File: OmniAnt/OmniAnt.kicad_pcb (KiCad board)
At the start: 2 copper layers, 1 part, among them U1 ESP32-S3-WROOM-1

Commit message: Mostly organizing
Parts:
- added C1: 1uF, PCM_JLCPCB:C_0603, F.Cu at (-115.2, 17.5)
- added C11: 1uF, PCM_JLCPCB:C_0603, F.Cu at (-115.2, 24.2)
- added C14: 1uF, PCM_JLCPCB:C_0603, F.Cu at (-115.2, 26.5)
- added C15: 100nF, PCM_JLCPCB:C_0603, F.Cu at (-115.2, 37.5)
- added C19: 1uF, PCM_JLCPCB:C_0603, F.Cu at (-115.2, 28.8)
- added C2: 1uF, PCM_JLCPCB:C_0603, F.Cu at (-115.2, 19.8)
- added C20: 1uF, PCM_JLCPCB:C_0603, F.Cu at (-115.2, 31.0)
- added C21: 100nF, PCM_JLCPCB:C_0603, F.Cu at (-115.2, 33.2)
- added C22: 100nF, PCM_JLCPCB:C_0603, F.Cu at (-115.2, 39.8)
- added C23: 100nF, PCM_JLCPCB:C_0603, F.Cu at (-115.2, 42.0)
- added C4: 470pF, PCM_JLCPCB:C_0603, F.Cu at (-115.2, 22.0)
- added C6: 10uF, PCM_JLCPCB:C_0805, F.Cu at (-108.2, 27.5)
- added C7: 10uF, PCM_JLCPCB:C_0805, F.Cu at (-111.1, 43.5)
- added C8: 10uF, PCM_JLCPCB:C_0805, F.Cu at (-108.2, 30.5)
- added D1: PMEG100V080ELPD, Package_TO_SOT_SMD:Nexperia_CFP15_SOT-1289, F.Cu at (-56.0, 42.9)
- added J1: Conn_01x02_Pin, Connector_PinHeader_1.27mm:PinHeader_1x02_P1.27mm_Vertical, F.Cu at (-62.6, 44.1)
- added J3: Connector, USB-TYPE-C-16P, PCM_JLCPCB:TYPE-C-SMD_HX-TYPE-C-16PIN, F.Cu at (-54.8, 34.0)
- added Q10: NTMFS4C324NT1G, Footprints:NVMFS5C442NLWFAFT1G, F.Cu at (-91.7, 21.2)
- added Q11: NTMFS4C324NT1G, Footprints:NVMFS5C442NLWFAFT1G, F.Cu at (-83.0, 21.2)
- added Q12: NTMFS4C324NT1G, Footprints:NVMFS5C442NLWFAFT1G, F.Cu at (-74.4, 21.2)
- added Q7: NTMFS4C324NT1G, Footprints:NVMFS5C442NLWFAFT1G, F.Cu at (-64.0, 21.7)
- added Q8: NTMFS4C324NT1G, Footprints:NVMFS5C442NLWFAFT1G, F.Cu at (-109.0, 21.2)
- added Q9: NTMFS4C324NT1G, Footprints:NVMFS5C442NLWFAFT1G, F.Cu at (-100.3, 21.2)
- added R1: 10kΩ, PCM_JLCPCB:R_0402, F.Cu at (-111.9, 37.3)
- added R10: 5.1kΩ, PCM_JLCPCB:R_0402, F.Cu at (-111.9, 32.4)
- added R11: 5.1kΩ, PCM_JLCPCB:R_0402, F.Cu at (-111.9, 39.1)
- added R12: 5.1kΩ, PCM_JLCPCB:R_0402, F.Cu at (-111.9, 41.0)
- added R3: 10kΩ, PCM_JLCPCB:R_0402, F.Cu at (-111.9, 26.9)
- added R4: 10kΩ, PCM_JLCPCB:R_0402, F.Cu at (-111.9, 28.7)
- added R6: 2m, Resistor_SMD:R_1206_3216Metric, F.Cu at (-35.3, 32.0)
- added R9: 5.1kΩ, PCM_JLCPCB:R_0402, F.Cu at (-111.9, 30.6)
- added U2: TPSM53603RDA, Package_DFN_QFN:Texas_B3QFN-14-1EP_5x5.5mm_P0.65mm_ThermalVia, F.Cu at (-48.0, 43.3)
- added U3: MCF8329A1IREER, Footprints:REE0036A-MFG, F.Cu at (8.50, 144.0)
- added U4: USBLC6-2P6, Package_TO_SOT_SMD:SOT-666, F.Cu at (-58.2, 47.6)
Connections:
- U1 pad 12: unconnected-(U1-IO8-Pad12) -> /MotorController_MCF8329A/SDA
- U1 pad 13: unconnected-(U1-USB_D--Pad13) -> /D-
- U1 pad 14: unconnected-(U1-USB_D+-Pad14) -> /D+
- U1 pad 17: unconnected-(U1-IO9-Pad17) -> /MotorController_MCF8329A/SCL
- U1 pad 2: unconnected-(U1-3V3-Pad2) -> +3.3V
- U1 pad 27: unconnected-(U1-IO0-Pad27) -> Net-(J1-Pin_1)
- U1 pad 4: unconnected-(U1-IO4-Pad4) -> /MotorController_MCF8329A/DACOut

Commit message: Good progress on the power stage today.
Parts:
- removed D1: PMEG100V080ELPD, Package_TO_SOT_SMD:Nexperia_CFP15_SOT-1289
- added D2: SSL34F, PCM_JLCPCB:D_SMAF, F.Cu at (-96.5, 99.0)
- moved Q8 34.6 mm to (-74.4, 19.5)
- moved Q7 15.1 mm to (-74.4, 10.7)
- moved Q12 13.4 mm to (-87.5, 18.7)
- moved Q11 11.9 mm to (-87.5, 10.2)
- moved Q9 8.46 mm to (-98.1, 13.0)
- moved Q10 6.68 mm to (-98.1, 23.0)

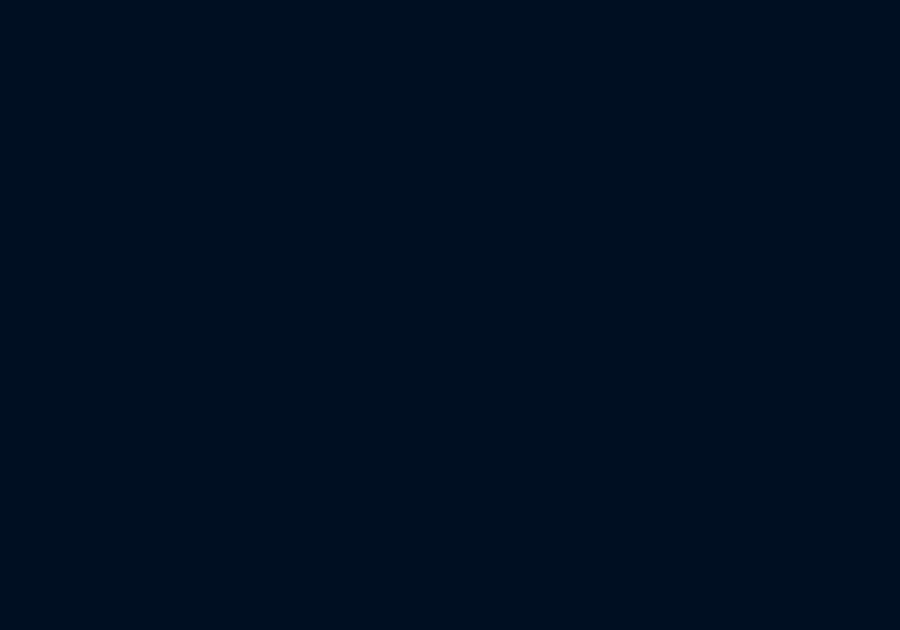
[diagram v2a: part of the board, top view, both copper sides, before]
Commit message: I added a green LED.
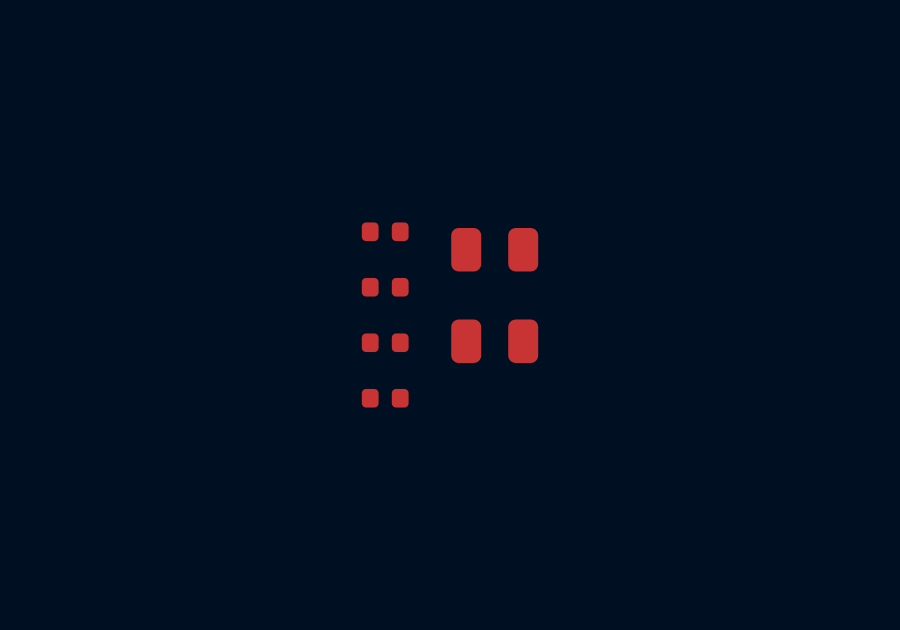
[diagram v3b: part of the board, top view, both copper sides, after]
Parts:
- added C10: 10uF, PCM_JLCPCB:C_0805, F.Cu at (-5.35, 34.1)
- added C9: 10uF, PCM_JLCPCB:C_0805, F.Cu at (-5.35, 31.1)
- added R13: 5.1kΩ, PCM_JLCPCB:R_0402, F.Cu at (-9.00, 34.1)
- added R14: 5.1kΩ, PCM_JLCPCB:R_0402, F.Cu at (-9.00, 36.0)
- added R2: 5.1kΩ, PCM_JLCPCB:R_0402, F.Cu at (-9.00, 30.4)
- added R5: 12kΩ, PCM_JLCPCB:R_0402, F.Cu at (-9.00, 32.3)
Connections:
- C23 pad 1: Net-(J2-VBUS) -> /VUSB
- D2 pad 1: /VUSB -> /Batt
- D2 pad 2: Net-(J2-VBUS) -> /VUSB
- J3 pad A12B1: Net-(J3-GND-PadA12B1) -> GND
- J3 pad A5: unconnected-(J3-CC1-PadA5) -> Net-(J3-CC1)
- J3 pad A6: unconnected-(J3-D+-PadA6) -> Net-(J3-D+-PadA6)
- J3 pad A7: unconnected-(J3-D--PadA7) -> Net-(J3-D--PadA7)
- J3 pad A9B4: Net-(J3-VBUS-PadA9B4) -> /VUSB
- J3 pad B12A1: Net-(J3-GND-PadA12B1) -> GND
- J3 pad B5: unconnected-(J3-CC2-PadB5) -> Net-(J3-CC2)
- J3 pad B6: unconnected-(J3-D+-PadB6) -> Net-(J3-D+-PadA6)
- J3 pad B7: unconnected-(J3-D--PadB7) -> Net-(J3-D--PadA7)
- J3 pad B9A4: Net-(J3-VBUS-PadA9B4) -> /VUSB
- J3 pad S1: unconnected-(J3-SHIELD-PadS1) -> GND
- R11 pad 1: /MotorController_MCF8329A/SCL -> /I2C_SCL
- R12 pad 1: /MotorController_MCF8329A/SDA -> /I2C_SDA
- U1 pad 10: unconnected-(U1-IO17-Pad10) -> /Motor1_PWM
- U1 pad 11: unconnected-(U1-IO18-Pad11) -> /Motor2_PWM
- U1 pad 12: /MotorController_MCF8329A/SDA -> unconnected-(U1-IO8-Pad12)
- U1 pad 17: /MotorController_MCF8329A/SCL -> unconnected-(U1-IO9-Pad17)
- U1 pad 23: unconnected-(U1-IO21-Pad23) -> /Motor3_PWM
- U1 pad 24: unconnected-(U1-IO47-Pad24) -> /I2C_SDA
- U1 pad 25: unconnected-(U1-IO48-Pad25) -> /I2C_SCL
- U1 pad 32: unconnected-(U1-IO39-Pad32) -> /SPI1_MOSI
- U1 pad 33: unconnected-(U1-IO40-Pad33) -> /SPI1_MISO
- U1 pad 34: unconnected-(U1-IO41-Pad34) -> /SPI1_SCK
- U1 pad 35: unconnected-(U1-IO42-Pad35) -> /SPI1_CS
- U1 pad 38: unconnected-(U1-IO2-Pad38) -> /Motor2_DAC
- U1 pad 39: unconnected-(U1-IO1-Pad39) -> /Motor1_DAC
- U1 pad 4: /MotorController_MCF8329A/DACOut -> /Motor3_DAC
- U2 pad 1: Net-(U2-VIN-Pad1) -> /Batt
- U2 pad 10: Net-(U2-PGND-Pad10) -> GND
- U2 pad 11: Net-(U2-PGND-Pad10) -> GND
- U2 pad 12: unconnected-(U2-AGND-Pad12) -> GND
- U2 pad 14: Net-(U2-VIN-Pad1) -> /Batt
- U2 pad 15: Net-(U2-PGND-Pad10) -> GND
- U2 pad 2: unconnected-(U2-EN-Pad2) -> /Batt
- U2 pad 3: Net-(U2-PGND-Pad10) -> GND
- U2 pad 7: Net-(U2-VOUT-Pad7) -> +3.3V
- U2 pad 8: Net-(U2-VOUT-Pad7) -> +3.3V
- U2 pad 9: unconnected-(U2-FB-Pad9) -> Net-(U2-FB)
- U3 pad 27: /MotorController_MCF8329A/3.3V -> /Motor1_PWM
- U3 pad 29: /MotorController_MCF8329A/SDA -> /MotorController_MCF8329A/I2C_SDA
- U3 pad 30: /MotorController_MCF8329A/SCL -> /MotorController_MCF8329A/I2C_SCL
- U3 pad 33: /MotorController_MCF8329A/DACOut -> /Motor1_DAC
- U4 pad 1: Net-(J2-D-) -> Net-(J3-D+-PadA6)
- U4 pad 2: Net-(J2-VBUS) -> /VUSB
- U4 pad 3: Net-(J2-D+) -> Net-(J3-D--PadA7)
- U4 pad 4: /D+ -> /D-
- U4 pad 6: /D- -> /D+

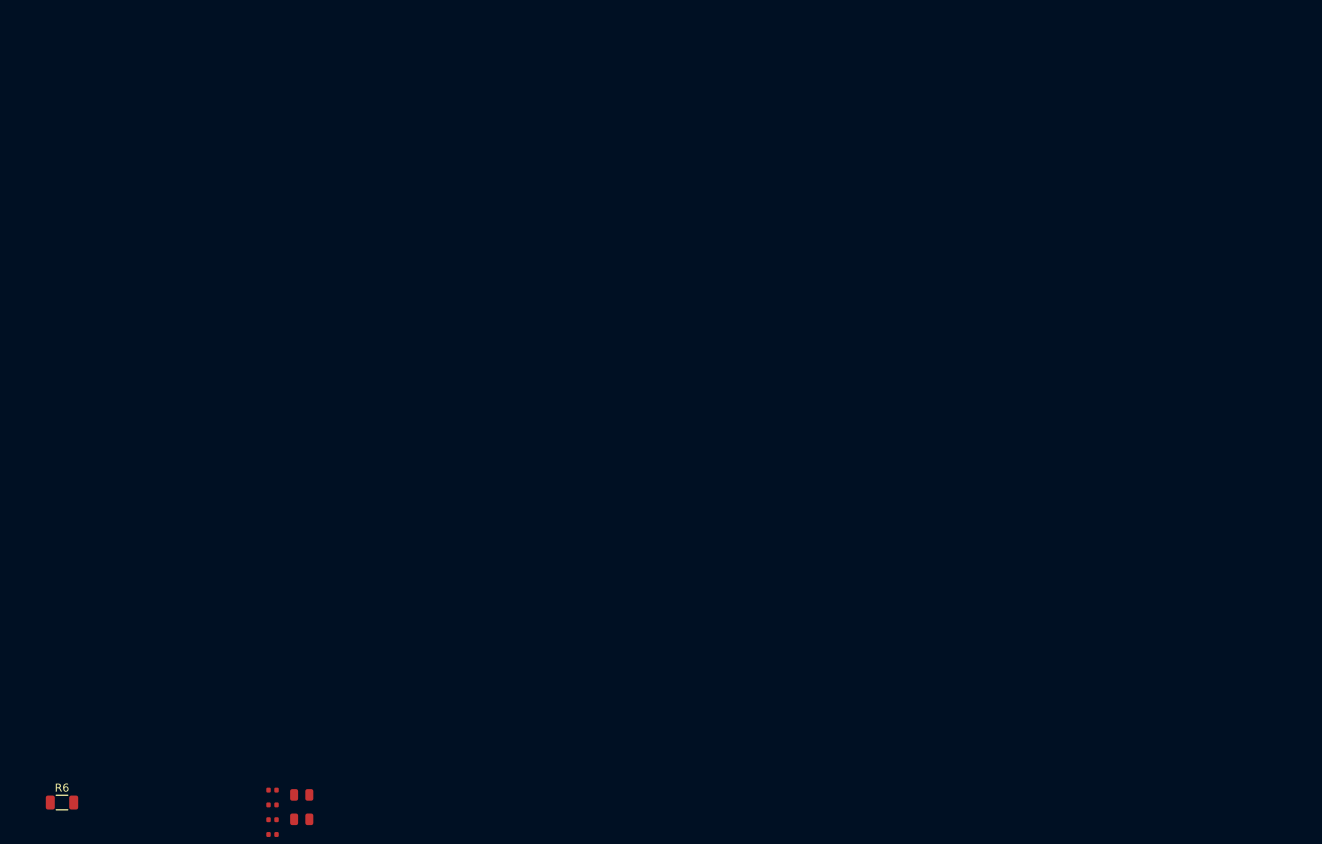
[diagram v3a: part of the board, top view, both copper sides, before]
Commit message: I added in the XT30 Connectors for the batteries
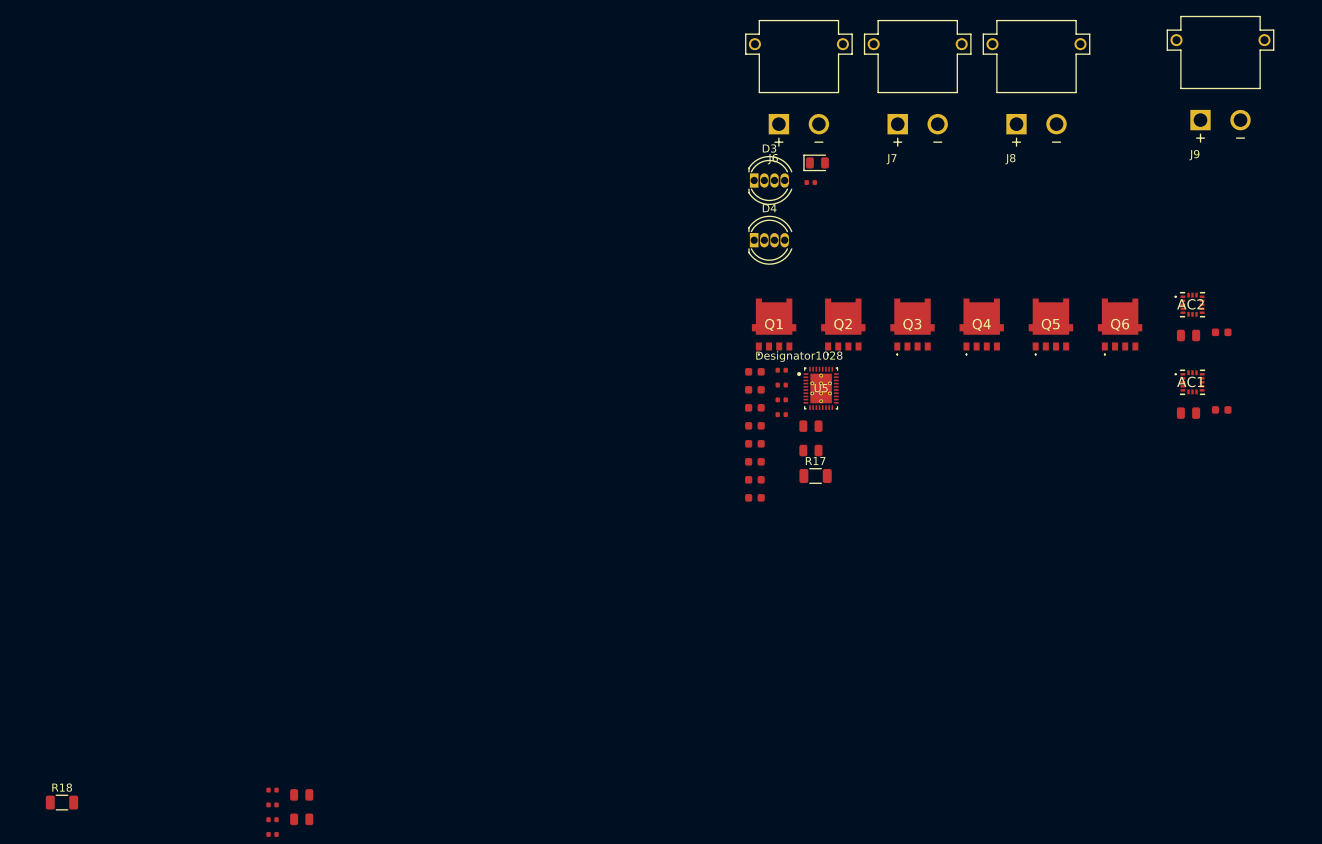
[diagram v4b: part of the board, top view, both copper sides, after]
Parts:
- added AC1: H3LIS331DL, Footprints:LIS3DHTR, F.Cu at (106.0, -20.5)
- added AC2: H3LIS331DL, Footprints:LIS3DHTR, F.Cu at (106.0, -30.2)
- added C1: 10uF, PCM_JLCPCB:C_0805, F.Cu at (105.5, -16.7)
- added C12: 10uF, PCM_JLCPCB:C_0805, F.Cu at (58.3, -15.0)
- added C13: 10uF, PCM_JLCPCB:C_0805, F.Cu at (58.3, -12.0)
- added C16: 100nF, PCM_JLCPCB:C_0603, F.Cu at (51.3, -17.3)
- added C17: 1uF, PCM_JLCPCB:C_0603, F.Cu at (51.3, -15.1)
- added C18: 470pF, PCM_JLCPCB:C_0603, F.Cu at (51.3, -12.8)
- added C2: 100nF, PCM_JLCPCB:C_0603, F.Cu at (109.7, -17.1)
- added C24: 1uF, PCM_JLCPCB:C_0603, F.Cu at (51.3, -10.6)
- added C25: 1uF, PCM_JLCPCB:C_0603, F.Cu at (51.3, -8.33)
- added C26: 1uF, PCM_JLCPCB:C_0603, F.Cu at (51.3, -6.08)
- added C3: 1uF, PCM_JLCPCB:C_0603, F.Cu at (51.3, -21.8)
- added C4: 100nF, PCM_JLCPCB:C_0603, F.Cu at (109.7, -26.8)
- added C5: 1uF, PCM_JLCPCB:C_0603, F.Cu at (51.3, -19.6)
- added C6: 10uF, PCM_JLCPCB:C_0805, F.Cu at (105.5, -26.4)
- added D1: Green, PCM_JLCPCB:D_0805, F.Cu at (59.1, -48.0)
- added D3: NeoPixel_THT, LED_THT:LED_D5.0mm-4_RGB, F.Cu at (51.2, -45.8)
- added D4: NeoPixel_THT, LED_THT:LED_D5.0mm-4_RGB, F.Cu at (51.2, -38.3)
- added J6: XT30PW-M, Footprints:AMASS_XT30PW-M, F.Cu at (56.8, -62.8)
- added J7: XT30PW-M, Footprints:AMASS_XT30PW-M, F.Cu at (71.7, -62.8)
- added J8: XT30PW-M, Footprints:AMASS_XT30PW-M, F.Cu at (86.5, -62.8)
- added J9: XT30PW-M, Footprints:AMASS_XT30PW-M, F.Cu at (109.5, -63.3)
- added Q1: NTMFS4C324NT1G, Footprints:NVMFS5C442NLWFAFT1G, F.Cu at (53.7, -27.8)
- added Q2: NTMFS4C324NT1G, Footprints:NVMFS5C442NLWFAFT1G, F.Cu at (62.4, -27.8)
- added Q3: NTMFS4C324NT1G, Footprints:NVMFS5C442NLWFAFT1G, F.Cu at (71.0, -27.8)
- added Q4: NTMFS4C324NT1G, Footprints:NVMFS5C442NLWFAFT1G, F.Cu at (79.7, -27.8)
- added Q5: NTMFS4C324NT1G, Footprints:NVMFS5C442NLWFAFT1G, F.Cu at (88.3, -27.8)
- added Q6: NTMFS4C324NT1G, Footprints:NVMFS5C442NLWFAFT1G, F.Cu at (97.0, -27.8)
- added R15: 5.1kΩ, PCM_JLCPCB:R_0402, F.Cu at (54.6, -18.3)
- added R16: 5.1kΩ, PCM_JLCPCB:R_0402, F.Cu at (54.6, -16.5)
- added R17: 2m, Resistor_SMD:R_1206_3216Metric, F.Cu at (58.9, -8.81)
- added R3: 33Ω, PCM_JLCPCB:R_0402, F.Cu at (58.3, -45.5)
- added R7: 10kΩ, PCM_JLCPCB:R_0402, F.Cu at (54.6, -22.0)
- added R8: 10kΩ, PCM_JLCPCB:R_0402, F.Cu at (54.6, -20.2)
- added U5: MCF8329A1IREER, Footprints:REE0036A-MFG, F.Cu at (59.6, -19.8)
- renumbered C2 to C11, C8 to C14, C6 to C19, C21 to C20, C11 to C21, C4 to C27, C14 to C28, C20 to C29, C19 to C30, C1 to C8, R6 to R18, R3 to R6
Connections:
- net /MotorController_MCF8329A/3.3V renamed /Motor1/3.3V
- net /MotorController_MCF8329A/Batt renamed /Motor1/Batt
- net /MotorController_MCF8329A/I2C_SCL renamed /Motor1/I2C_SCL
- net /MotorController_MCF8329A/I2C_SDA renamed /Motor1/I2C_SDA
- net /MotorController_MCF8329A/LSS renamed /Motor1/LSS
- U1 pad 20: unconnected-(U1-IO12-Pad20) -> /SPI2_SCK
- U1 pad 21: unconnected-(U1-IO13-Pad21) -> /SPI2_MOSI
- U1 pad 22: unconnected-(U1-IO14-Pad22) -> /SPI2_MISO
- U1 pad 28: unconnected-(U1-IO35-Pad28) -> /Rx_Channel1
- U1 pad 29: unconnected-(U1-IO36-Pad29) -> /Rx_Channel2
- U1 pad 30: unconnected-(U1-IO37-Pad30) -> /Rx_Channel3
- U1 pad 36: unconnected-(U1-RXD0-Pad36) -> /Accel2_INT
- U1 pad 37: unconnected-(U1-TXD0-Pad37) -> /Accel1_INT
- U1 pad 5: unconnected-(U1-IO5-Pad5) -> Net-(D3-DIN)
- U1 pad 8: unconnected-(U1-IO15-Pad8) -> /SPI2_CS
- U1 pad 9: unconnected-(U1-IO16-Pad9) -> Net-(U1-IO16)
